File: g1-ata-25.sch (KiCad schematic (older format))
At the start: 29 parts, among them P1 G1_DC_SOCKET, P2 G1_GD_PLUGNH, P3 IDE_40PIN, P4 IDE_44PIN, P5 CONN_01X02, P6 CONN_01X04, P7 BARREL_JACK, P8 CONN_01X05, U1 TCXO_DFAS11, U2 TS30011-M050

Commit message: Routing...
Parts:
- removed P7: BARREL_JACK, Connect:BARREL_JACK, symbol BARREL_JACK
- added P7: CONN_01X02, Sockets_WAGO734:WAGO_734_2pin_Straight_RuggedPads, symbol CONN_01X02
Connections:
- net CD_LRCK is gone; now on net ~CD_LRCK: P8.1 (P1)
- net GND: now also P7.2 (P2)
- net at F1.1: now also P7.1 (P1)
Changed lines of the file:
@@
-$EndComp
-$Comp
-L BARREL_JACK P7
-U 1 1 574D3BCC
-P 3750 4700
-F 0 "P7" H 3700 5000 50  0000 C CNN
-F 1 "BARREL_JACK" H 3731 4934 50  0001 C CNN
-F 2 "Connect:BARREL_JACK" H 3750 4700 50  0001 C CNN
-F 3 "" H 3750 4700 50  0000 C CNN
-F 4 "12VDC" H 3700 4900 60  0000 C CNN "Func"
-	1    3750 4700
-	1    0    0    -1
 $EndComp
 $Comp
@@
 	650  5100 750  5000
 Text Label 750  4700 0    60   ~ 0
-CD_LRCK
+~CD_LRCK
 Text Label 750  4800 0    60   ~ 0
 CD_SD
@@
 Wire Wire Line
 	4300 4600 4400 4600
-Connection ~ 4050 4800
 Wire Wire Line
 	4050 4700 4050 4900
@@
 Wire Wire Line
 	9800 4850 9800 4950
+$Comp
+L CONN_01X02 P7
+U 1 1 57506E84
+P 3850 4650
+F 0 "P7" H 3928 4645 50  0000 L CNN
+F 1 "CONN_01X02" H 3928 4600 50  0001 L CNN
+F 2 "Sockets_WAGO734:WAGO_734_2pin_Straight_RuggedPads" H 3850 4650 50  0001 C CNN
+F 3 "" H 3850 4650 50  0000 C CNN
+	1    3850 4650
+	-1   0    0    -1
+$EndComp
 $EndSCHEMATC

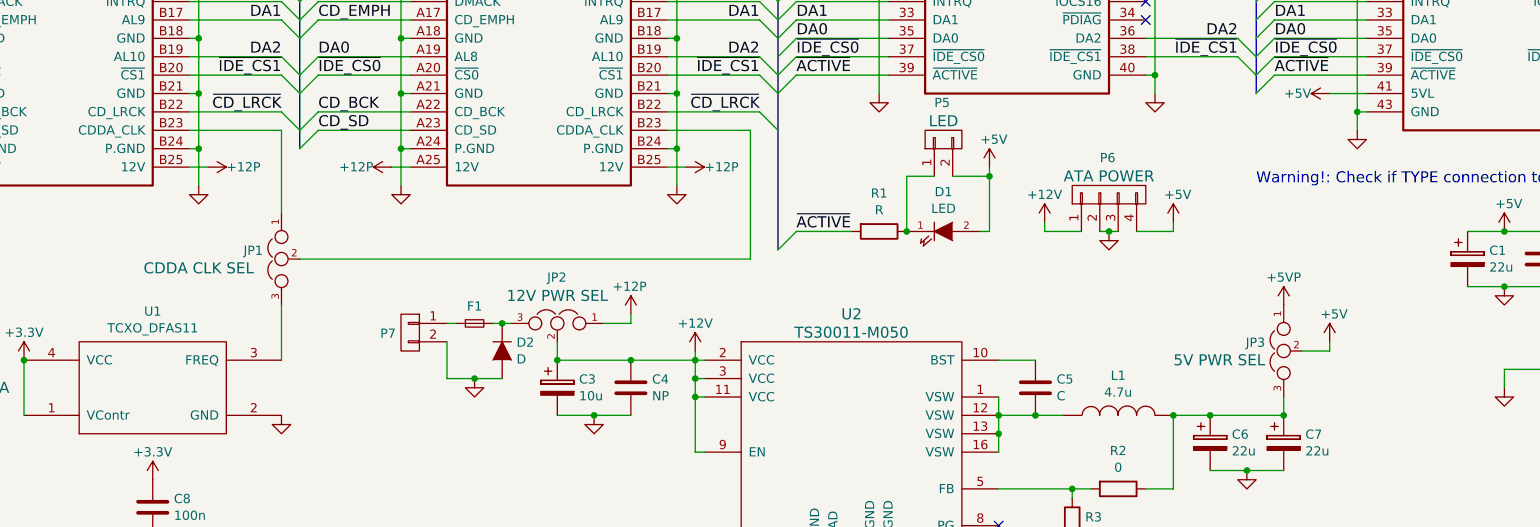
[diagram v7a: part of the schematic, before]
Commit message: Added an external 5V power source plus other tweaks.
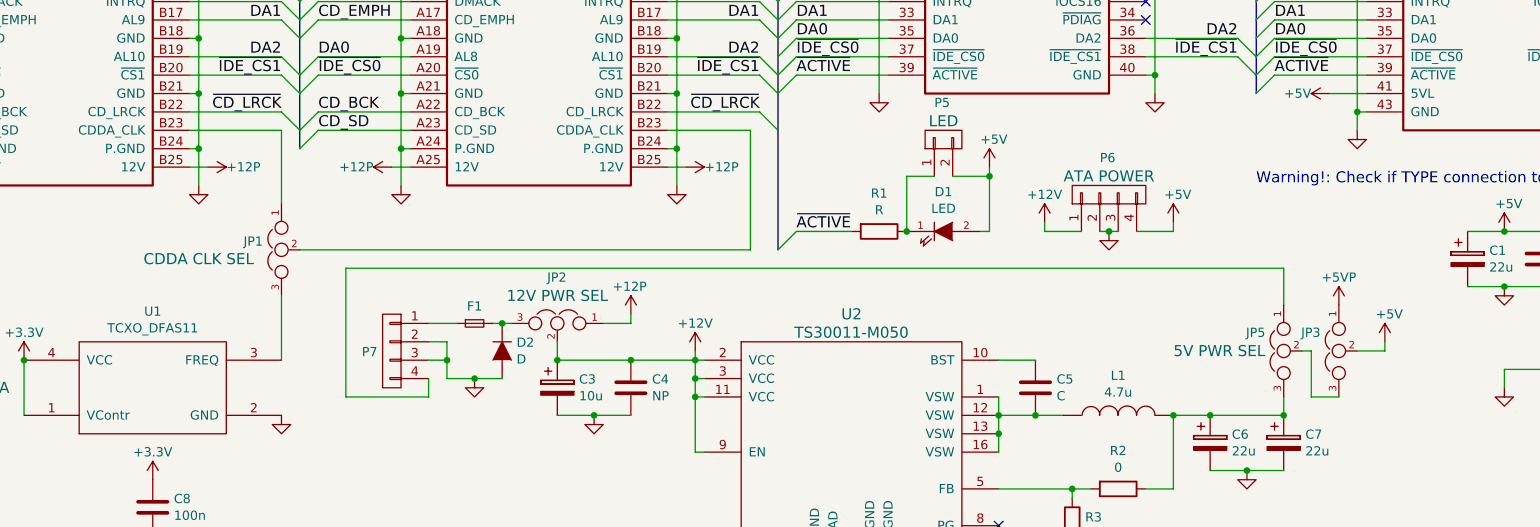
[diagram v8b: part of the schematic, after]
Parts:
- removed P7: CONN_01X02, Sockets_WAGO734:WAGO_734_2pin_Straight_RuggedPads, symbol CONN_01X02
- added JP5: JUMPER3, Pin_Headers:Pin_Header_Straight_1x03, symbol JUMPER3
- added P7: CONN_01X04, Sockets_MOLEX_KK-System:Socket_MOLEX-KK-RM3-96mm_Lock_4pin_straight, symbol CONN_01X04
- P5: footprint Socket_Strips:Socket_Strip_Straight_1x02 -> Sockets_MOLEX_KK-System:Socket_MOLEX-KK-RM2-54mm_Lock_2pin_straight
- P6: footprint Socket_Strips:Socket_Strip_Straight_1x04 -> Sockets_MOLEX_KK-System:Socket_MOLEX-KK-RM3-96mm_Lock_4pin_straight
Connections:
- net GND: now also P7.2 (P2), P7.3 (P3)
- net at C6.1, C7.1, L1.2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: now also JP5.3; no longer JP3.3
- net at F1.1: now also P7.1 (P1)
- new net: JP3.3, JP5.2
- new net: JP5.1, P7.4 (P4)
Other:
- moved on the sheet: JP1, JP3
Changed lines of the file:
@@
 L JUMPER3 JP1
 U 1 1 574C8107
-P 3150 4250
-F 0 "JP1" V 3104 4351 50  0000 L CNN
-F 1 "JUMPER3" V 3195 4351 50  0001 L CNN
-F 2 "Pin_Headers:Pin_Header_Straight_1x03" H 3150 4250 50  0001 C CNN
-F 3 "" H 3150 4250 50  0000 C CNN
-F 4 "CDDA CLK SEL" V 3200 4700 60  0000 C CNN "Func"
-	1    3150 4250
+P 3150 4200
+F 0 "JP1" V 3104 4301 50  0000 L CNN
+F 1 "JUMPER3" V 3195 4301 50  0001 L CNN
+F 2 "Pin_Headers:Pin_Header_Straight_1x03" H 3150 4200 50  0001 C CNN
+F 3 "" H 3150 4200 50  0000 C CNN
+F 4 "CDDA CLK SEL" V 3200 4650 60  0000 C CNN "Func"
+	1    3150 4200
 	0    -1   1    0
 $EndComp
@@
 L JUMPER3 JP3
 U 1 1 574CB39F
-P 8600 4750
-F 0 "JP3" V 8554 4851 50  0000 L CNN
-F 1 "JUMPER3" V 8645 4851 50  0001 L CNN
-F 2 "Pin_Headers:Pin_Header_Straight_1x03" H 8600 4750 50  0001 C CNN
-F 3 "" H 8600 4750 50  0000 C CNN
-F 4 "5V PWR SEL" V 8650 5100 60  0000 C CNN "Func"
-	1    8600 4750
+P 8900 4750
+F 0 "JP3" V 8800 4850 50  0000 L CNN
+F 1 "JUMPER3" V 8945 4851 50  0001 L CNN
+F 2 "Pin_Headers:Pin_Header_Straight_1x03" H 8900 4750 50  0001 C CNN
+F 3 "" H 8900 4750 50  0000 C CNN
+F 4 "5V PWR SEL" V 8950 5100 60  0001 C CNN "Func"
+	1    8900 4750
 	0    -1   1    0
 $EndComp
@@
 L +5V #PWR025
 U 1 1 574CB755
-P 8850 4700
-F 0 "#PWR025" H 8850 4550 50  0001 C CNN
-F 1 "+5V" H 8800 4850 50  0000 L CNN
-F 2 "" H 8850 4700 50  0000 C CNN
-F 3 "" H 8850 4700 50  0000 C CNN
-	1    8850 4700
+P 9150 4700
+F 0 "#PWR025" H 9150 4550 50  0001 C CNN
+F 1 "+5V" H 9100 4850 50  0000 L CNN
+F 2 "" H 9150 4700 50  0000 C CNN
+F 3 "" H 9150 4700 50  0000 C CNN
+	1    9150 4700
 	1    0    0    -1
 $EndComp
@@
 L +5VP #PWR026
 U 1 1 574D225D
-P 8600 4500
-F 0 "#PWR026" H 8600 4350 50  0001 C CNN
-F 1 "+5VP" H 8600 4650 50  0000 C CNN
-F 2 "" H 8600 4500 50  0000 C CNN
-F 3 "" H 8600 4500 50  0000 C CNN
-	1    8600 4500
+P 8900 4500
+F 0 "#PWR026" H 8900 4350 50  0001 C CNN
+F 1 "+5VP" H 8900 4650 50  0000 C CNN
+F 2 "" H 8900 4500 50  0000 C CNN
+F 3 "" H 8900 4500 50  0000 C CNN
+	1    8900 4500
 	1    0    0    -1
 $EndComp
@@
 F 0 "P6" V 7850 3950 50  0000 R CNN
 F 1 "CONN_01X04" V 7524 3662 50  0001 R CNN
-F 2 "Socket_Strips:Socket_Strip_Straight_1x04" H 7650 3900 50  0001 C CNN
+F 2 "Sockets_MOLEX_KK-System:Socket_MOLEX-KK-RM3-96mm_Lock_4pin_straight" H 7650 3900 50  0001 C CNN
 F 3 "" H 7650 3900 50  0000 C CNN
 F 4 "ATA POWER" V 7750 3900 60  0000 C CNN "Func"
@@
 F 0 "P5" V 6950 3650 50  0000 R CNN
 F 1 "CONN_01X02" V 6624 3462 50  0001 R CNN
-F 2 "Socket_Strips:Socket_Strip_Straight_1x02" H 6750 3600 50  0001 C CNN
+F 2 "Sockets_MOLEX_KK-System:Socket_MOLEX-KK-RM2-54mm_Lock_2pin_straight" H 6750 3600 50  0001 C CNN
 F 3 "" H 6750 3600 50  0000 C CNN
 F 4 "LED" V 6850 3600 60  0000 C CNN "Func"
@@
 Connection ~ 4350 4600
 Wire Wire Line
-	4050 4600 4100 4600
+	3950 4600 4100 4600
 Wire Wire Line
 	4300 4600 4400 4600
@@
 	5400 4750 5400 5300
 Wire Wire Line
-	8850 4750 8850 4700
-Wire Wire Line
-	8700 4750 8850 4750
+	9150 4750 9150 4700
+Wire Wire Line
+	9000 4750 9150 4750
 Connection ~ 8600 5100
 Wire Wire Line
@@
 	5400 5300 5450 5300
 Wire Wire Line
-	3150 3550 3150 4000
+	3150 3550 3150 3950
 Wire Wire Line
 	5700 3550 5250 3550
 Wire Wire Line
-	5700 4250 5700 3550
-Wire Wire Line
-	3250 4250 5700 4250
+	5700 4200 5700 3550
+Wire Wire Line
+	3250 4200 5700 4200
 Wire Wire Line
 	2650 3550 3150 3550
 Wire Wire Line
-	3150 4500 3150 4800
+	3150 4450 3150 4800
 Connection ~ 1750 4800
 Wire Wire Line
@@
 	9800 4850 9800 4950
 $Comp
-L CONN_01X02 P7
-U 1 1 57506E84
-P 3850 4650
-F 0 "P7" H 3928 4645 50  0000 L CNN
-F 1 "CONN_01X02" H 3928 4600 50  0001 L CNN
-F 2 "Sockets_WAGO734:WAGO_734_2pin_Straight_RuggedPads" H 3850 4650 50  0001 C CNN
-F 3 "" H 3850 4650 50  0000 C CNN
-	1    3850 4650
+L CONN_01X04 P7
+U 1 1 5759007C
+P 3750 4750
+F 0 "P7" H 3828 4745 50  0000 L CNN
+F 1 "CONN_01X04" H 3828 4700 50  0001 L CNN
+F 2 "Sockets_MOLEX_KK-System:Socket_MOLEX-KK-RM3-96mm_Lock_4pin_straight" H 3750 4750 50  0001 C CNN
+F 3 "" H 3750 4750 50  0000 C CNN
+	1    3750 4750
 	-1   0    0    -1
 $EndComp
+Wire Wire Line
+	3950 4700 4050 4700
+Wire Wire Line
+	3950 4800 4050 4800
+Connection ~ 4050 4800
+Wire Wire Line
+	3950 4900 3950 5000
+Wire Wire Line
+	3950 5000 3500 5000
+Wire Wire Line
+	3500 5000 3500 4300
+Wire Wire Line
+	3500 4300 8600 4300
+$Comp
+L JUMPER3 JP5
+U 1 1 575912D5
+P 8600 4750
+F 0 "JP5" V 8500 4850 50  0000 L CNN
+F 1 "JUMPER3" V 8645 4851 50  0001 L CNN
+F 2 "Pin_Headers:Pin_Header_Straight_1x03" H 8600 4750 50  0001 C CNN
+F 3 "" H 8600 4750 50  0000 C CNN
+F 4 "5V PWR SEL" V 8600 5100 60  0000 C CNN "Func"
+	1    8600 4750
+	0    -1   1    0
+$EndComp
+Wire Wire Line
+	8600 4300 8600 4500
+Wire Wire Line
+	8900 5000 8750 5000
+Wire Wire Line
+	8750 5000 8750 4750
+Wire Wire Line
+	8750 4750 8700 4750
 $EndSCHEMATC
